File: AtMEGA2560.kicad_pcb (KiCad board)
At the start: 4 copper layers, 101.6 x 53.3 mm, 60 parts, among them IC1 NCP1117-5.0_SOT223, IC3 ATmega2560-16AU, IC4 ATmega16U2-AU, IC6 LP2985-3.3, IC7 LMV358IDGKR, T1 FDN340P, X1 DC21MMX, X2 USB-B_TH, Y1 CSTCE16M0V53-R0 16MHZ, Y2 16MHz

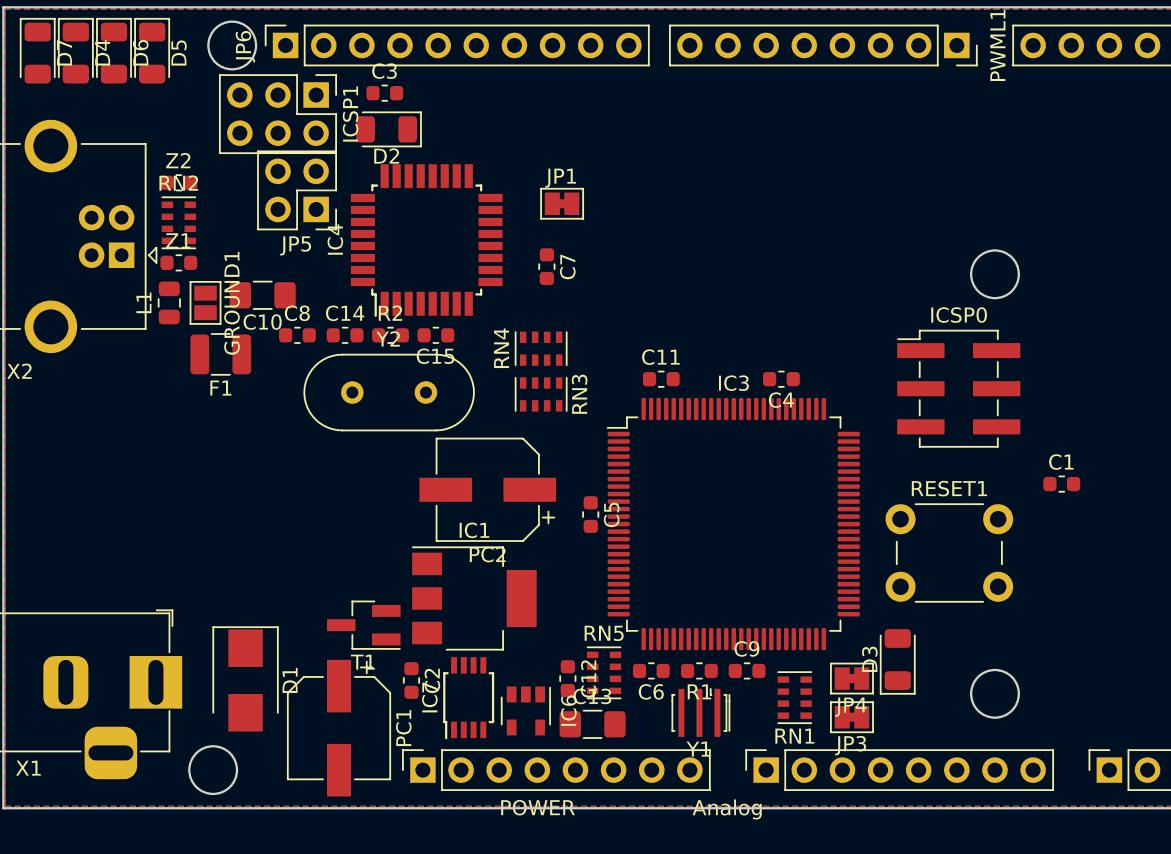
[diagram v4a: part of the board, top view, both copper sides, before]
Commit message: Orthogonal to digital plane  analog routing on prefered plane
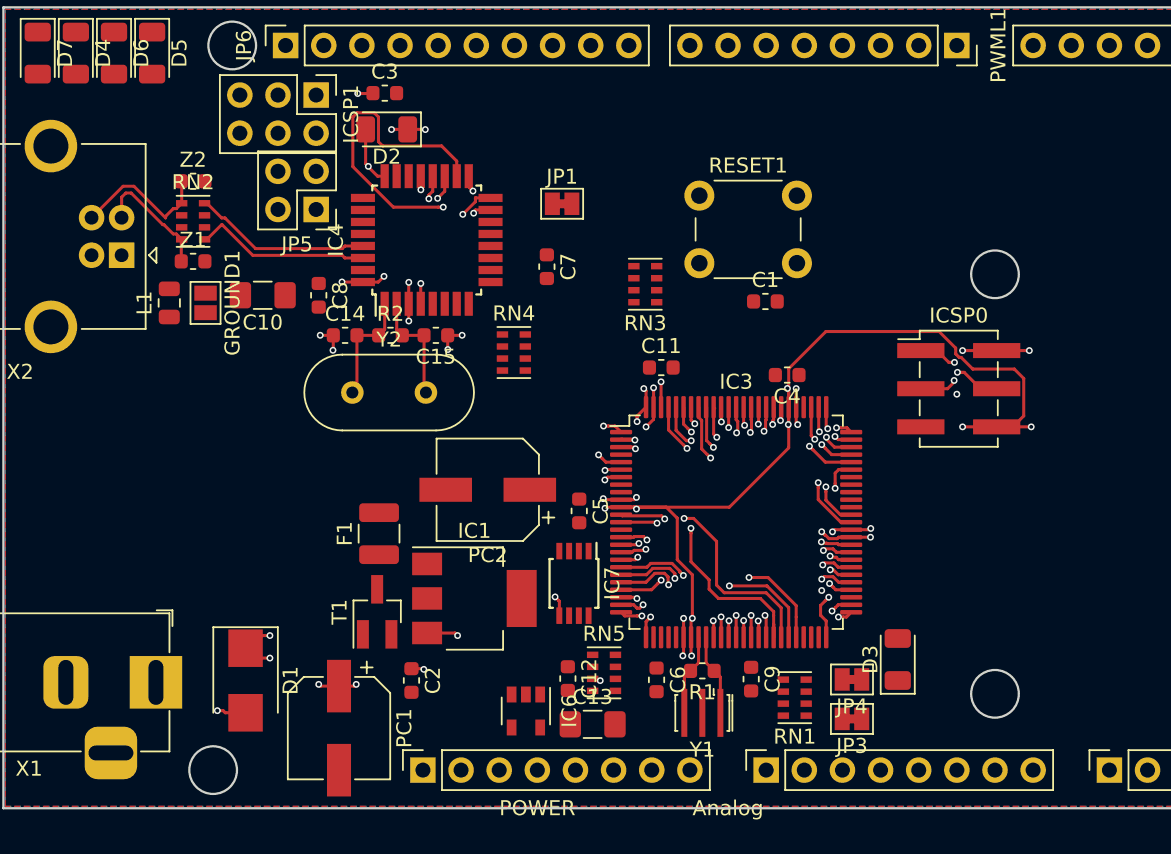
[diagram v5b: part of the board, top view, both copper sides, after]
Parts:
- moved RESET1 25.4 mm to (122.5, 81.1)
- moved C1 23.2 mm to (127.0, 88.2)
- moved F1 15.9 mm to (101.2, 103.6), turned to 90 degrees
- moved IC7 10.3 mm to (114.2, 106.9), turned to 270 degrees
- moved RN3 10.1 mm to (119.0, 87.0), turned to 180 degrees
- moved C8 3.02 mm to (97.2, 87.8), turned to 270 degrees
- moved RN4 1.83 mm to (110.2, 91.6), turned to 0 degrees
- moved T1 1.26 mm to (101.1, 108.8), turned to 90 degrees
- moved RN2 0.96 mm to (88.8, 82.8)
- moved Z1 0.96 mm to (88.8, 85.5)
- moved Z2 0.96 mm to (88.8, 80.2)
- moved C5 0.80 mm to (114.5, 102.1)
- moved C11 0.78 mm to (120.0, 92.6)
- moved C6 0.69 mm to (119.7, 113.4), turned to 270 degrees
- moved C9 0.61 mm to (126.0, 113.3), turned to 270 degrees
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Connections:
- net Net-(IC4-Pad29) renamed /USB1+
- net Net-(IC4-Pad30) renamed /USB1-
- net Net-(RN2-Pad1) renamed /USB2+
- net Net-(RN2-Pad4) renamed /USB2-
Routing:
- net SCL: track 0.00 -> 141.9 mm, vias 0 -> 1
- net SDA: track 0.00 -> 133.1 mm, vias 0 -> 1
- net PA6: track 0.00 -> 96.5 mm, vias 0 -> 1
- net GND: track 0.00 -> 74.7 mm, vias 0 -> 18
- net TXD3: track 0.00 -> 73.5 mm, vias 0 -> 1
- net MOSI: track 0.00 -> 73.4 mm, vias 0 -> 2
- net RXD3: track 0.00 -> 72.7 mm, vias 0 -> 1
- net /RXD1: track 0.00 -> 70.9 mm, vias 0 -> 1
- net /TXD1: track 0.00 -> 70.4 mm, vias 0 -> 1
- net MISO: track 0.00 -> 70.1 mm, vias 0 -> 2
- net SCK: track 0.00 -> 69.4 mm, vias 0 -> 2
- net ~SS~: track 0.00 -> 69.0 mm, vias 0 -> 2
- net PG2: track 0.00 -> 64.7 mm, vias 0 -> 1
- net PL0: track 0.00 -> 60.4 mm, vias 0 -> 1
- net PL2: track 0.00 -> 57.1 mm, vias 0 -> 1
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- added copper zone on In2.Cu, net +5V
- added copper zone on In1.Cu, net +VDC
- added copper zone on In1.Cu, net GND
- added copper zone on In1.Cu, net Net-(D1-Pad2)

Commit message: More of the digital routing done
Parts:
- moved RESET1 44.4 mm to (157.3, 108.8), turned to 180 degrees
- moved JP1 21.4 mm to (132.5, 91.3), turned to 270 degrees
- moved C7 19.5 mm to (131.7, 88.6), turned to 180 degrees
- moved C1 17.8 mm to (138.3, 101.8), turned to 180 degrees
- moved D3 12.7 mm to (138.3, 99.6), turned to 180 degrees
- moved RN3 8.73 mm to (111.5, 82.5), turned to 0 degrees
- moved C5 6.89 mm to (111.3, 96.0), turned to 180 degrees
- moved C6 0.70 mm to (119.7, 114.1)
- turned IC7 to 90 degrees
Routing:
- net ~RESET~: track 0.00 -> 79.6 mm, vias 0 -> 7
- net PA6: track 96.5 -> 48.7 mm
- net ~RESET2~: track 15.1 -> 57.5 mm, vias 1 -> 2
- net Net-(D7-Pad2): track 0.00 -> 39.4 mm, vias 0 -> 2
- net +5V: track 24.3 -> 63.6 mm, vias 17 -> 38
- net Net-(D4-Pad2): track 0.00 -> 36.8 mm, vias 0 -> 2
- net Net-(IC7-Pad6): track 0.00 -> 27.7 mm, vias 0 -> 2
- net ~HWB~: track 0.00 -> 24.9 mm, vias 0 -> 2
- net RXD0: track 37.6 -> 56.0 mm, vias 1 -> 2
- net /8PB4: track 29.3 -> 11.0 mm
- net TXD0: track 38.0 -> 56.3 mm, vias 1 -> 2
- net +3V3: track 0.00 -> 16.9 mm
- net Net-(IC7-Pad1): track 0.00 -> 15.0 mm, vias 0 -> 2
- net +VDC: track 20.7 -> 29.8 mm, vias 7 -> 8
- net Net-(C12-Pad1): track 0.00 -> 8.08 mm, vias 0 -> 2
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
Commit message: More of the digital routing done
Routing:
- net Net-(D6-Pad2): track 0.00 -> 38.2 mm, vias 0 -> 2
- net Net-(D5-Pad2): track 0.00 -> 36.1 mm, vias 0 -> 2
- net Net-(D6-Pad1): track 0.00 -> 35.3 mm, vias 0 -> 2
- net Net-(D5-Pad1): track 0.00 -> 32.7 mm, vias 0 -> 2
- net Net-(D4-Pad2): track 36.8 -> 39.8 mm
- net Net-(D7-Pad2): track 39.4 -> 41.6 mm
- net ~RESET2~: track 57.5 -> 58.5 mm

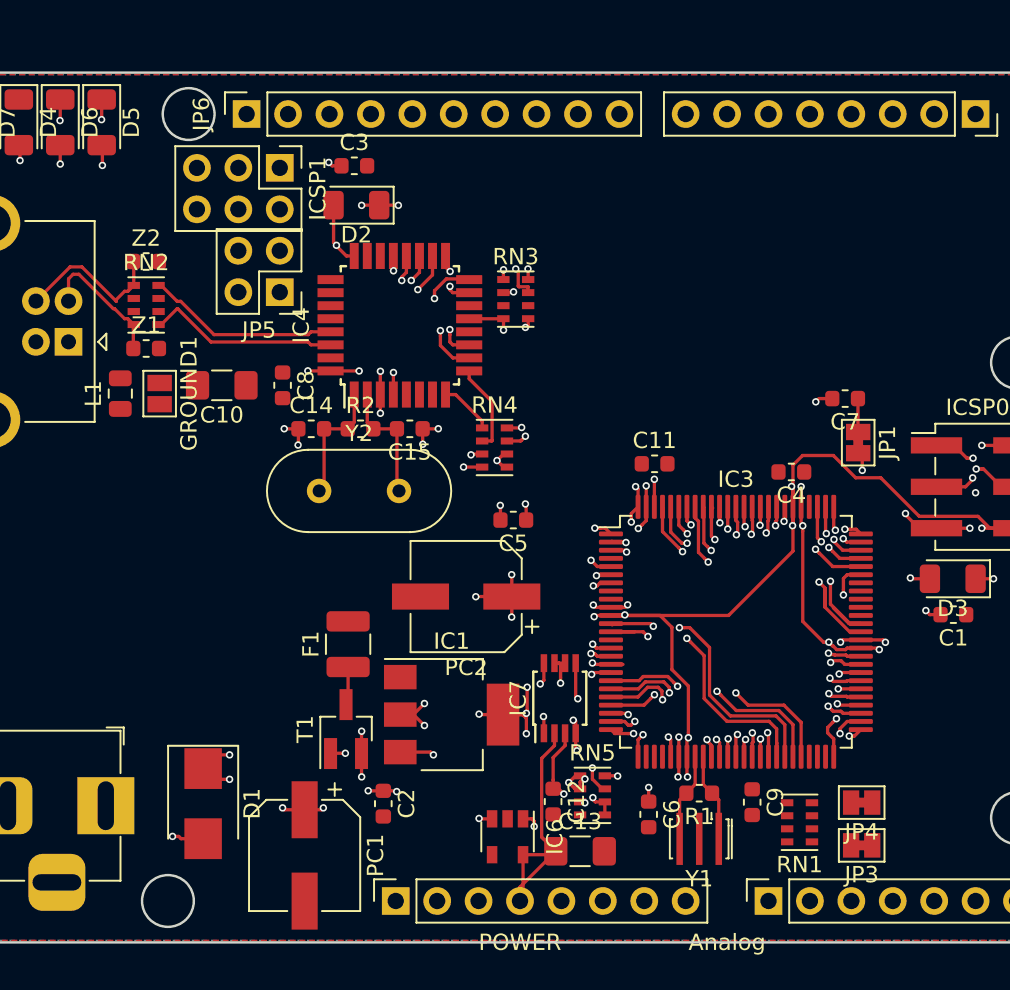
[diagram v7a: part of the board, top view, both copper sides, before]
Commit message: More of the USB-PSU routing done
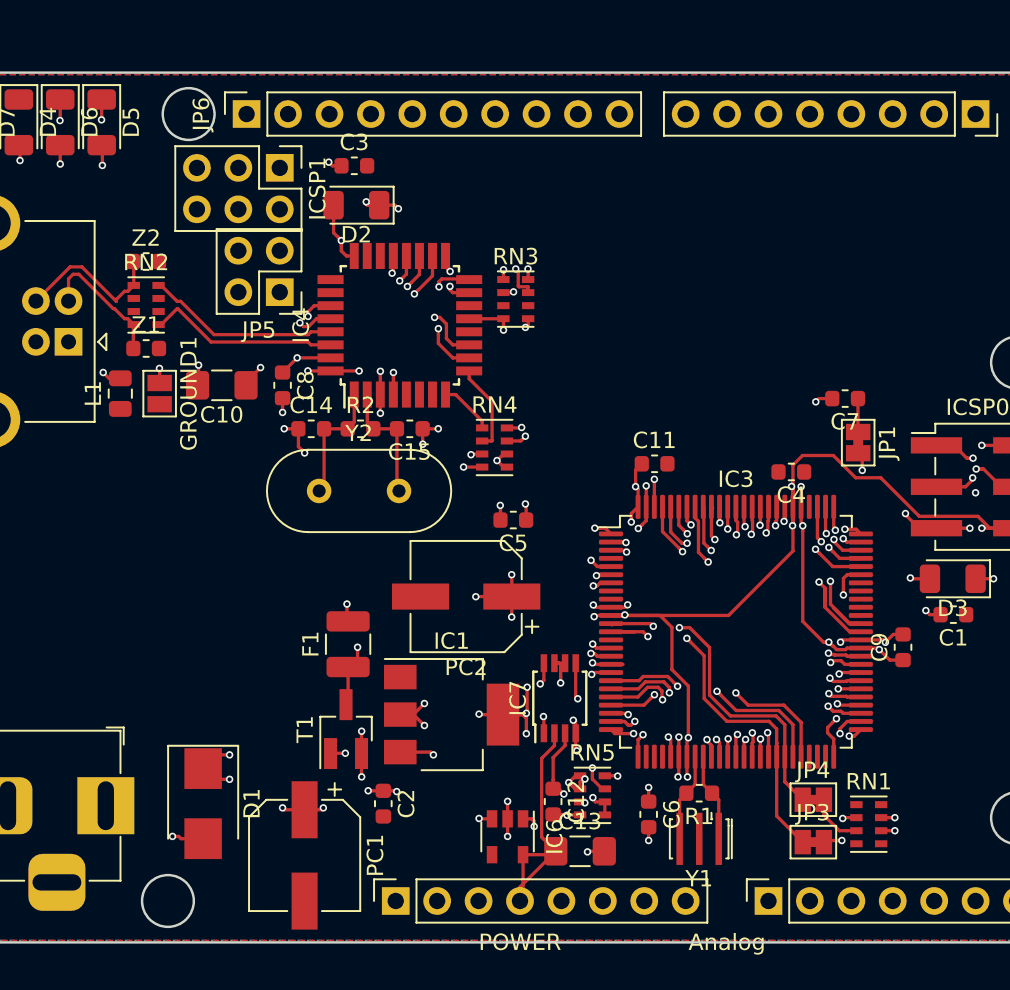
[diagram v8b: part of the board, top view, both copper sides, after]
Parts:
- moved C9 13.3 mm to (135.2, 103.8), turned to 90 degrees
- moved RN1 4.25 mm to (133.2, 114.7), turned to 0 degrees
- moved JP3 2.97 mm to (129.8, 115.8), turned to 0 degrees
- moved JP4 2.97 mm to (129.8, 113.2), turned to 0 degrees
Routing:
- net Net-(F1-Pad2): track 0.00 -> 29.3 mm, vias 0 -> 1
- net Net-(C10-Pad2): track 0.00 -> 26.3 mm, vias 0 -> 4
- net USBVCC: track 2.36 -> 26.6 mm, vias 0 -> 2
- net GND: track 71.4 -> 79.9 mm, vias 22 -> 28
- net Net-(C10-Pad1): track 0.00 -> 7.89 mm, vias 0 -> 2
- net SCL: track 141.8 -> 147.3 mm
- net +5V: track 63.8 -> 68.7 mm, vias 38 -> 40
- net Net-(JP3-Pad2): track 0.00 -> 3.37 mm, vias 0 -> 2
- net Net-(JP4-Pad2): track 0.00 -> 3.34 mm
- net SDA: track 132.4 -> 135.2 mm
- net Net-(D7-Pad2): track 41.6 -> 44.0 mm
- net PG2: track 64.2 -> 62.8 mm
- net Net-(D5-Pad1): track 32.7 -> 33.9 mm
- net Net-(D6-Pad1): track 35.3 -> 34.6 mm
- net Net-(D5-Pad2): track 36.1 -> 36.9 mm
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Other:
- rule trace_min: 0.127 -> 0.1
- rule via_min_drill: 0.254 -> 0.2
- rule via_min_size: 0.4572 -> 0.45
